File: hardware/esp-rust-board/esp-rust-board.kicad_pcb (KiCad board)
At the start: 2 copper layers, 22.9 x 63.5 mm, 96 parts, among them J1 USB4105-GF-A, Q1 DMG3415U, SW1 SW_Push, SW2 SW_Push, U1 SHTC3, U2 ICM-42670-P, U3 ESP32-C3-MINI-1, U4 Rust_Board, U5 SY8088, U6 MCP73831T-2ACI/OT, Y1 32.768Hz

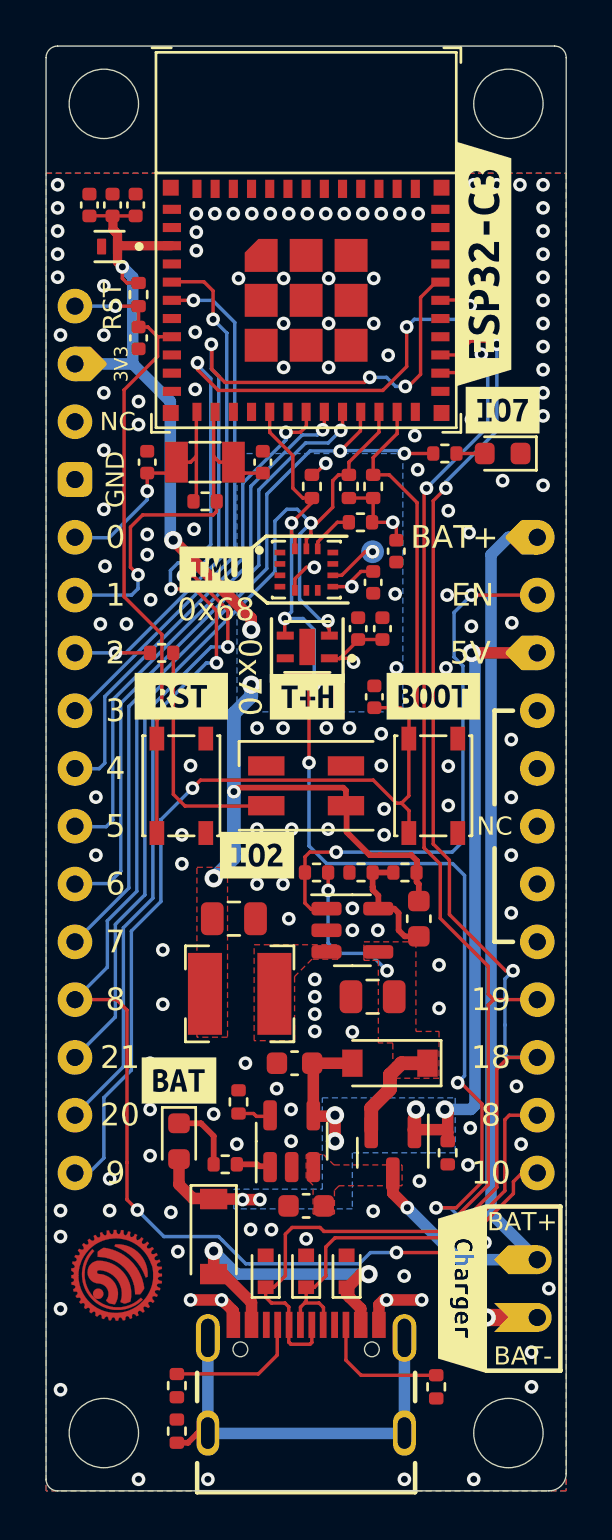
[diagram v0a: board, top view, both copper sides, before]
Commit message: Clean up, update symbols and footprints, port to Kicad 8.0
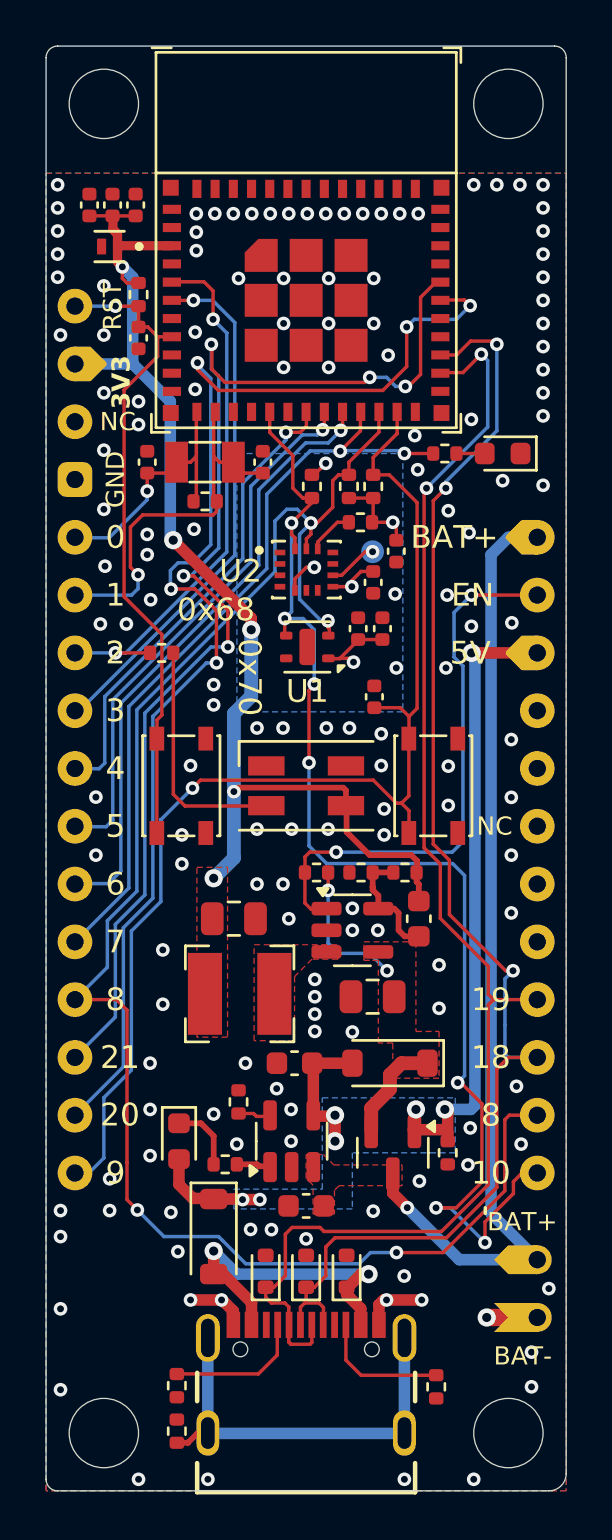
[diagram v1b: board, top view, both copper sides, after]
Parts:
- removed G***: LOGO, Rust_Board:esp-rs_logo_4mm
- removed G***: LOGO, Rust_Board:esp-rs_logo_tiny
- removed REF**: logo_HF, Rust_Board:logo_HF
- removed REF**: logo_HF, Rust_Board:logo_PB
- removed kibuzzard-61B9CCBB, kibuzzard-61B9CE3D, kibuzzard-61B9CE86, kibuzzard-61B9CEAB, kibuzzard-61B9EF98, kibuzzard-61C05335, kibuzzard-61C057D5, kibuzzard-61C057FD, kibuzzard-61C05804, kibuzzard-61C0588C, kibuzzard-61C05909, kibuzzard-61C05949, kibuzzard-61C05975, kibuzzard-61C0597E, kibuzzard-61C05A1A, kibuzzard-61C05A22, kibuzzard-61C05B60, kibuzzard-61C05BAC, kibuzzard-61C05C0D, kibuzzard-61C05C87, kibuzzard-61C05C92, kibuzzard-61C05D58, kibuzzard-61C05D75, kibuzzard-61C05DB0, kibuzzard-61C0F315, kibuzzard-61C0F325, kibuzzard-61C0F363, kibuzzard-61C0F3FF, kibuzzard-61C0F406, kibuzzard-61C0F511, kibuzzard-61C0F551: G***, label
- removed kibuzzard-61E1AB2E: G***, kibuzzard-61E1AB2E
- removed kibuzzard-61F26841: G***, kibuzzard-61F26841
- removed kibuzzard-61F26855: G***, kibuzzard-61F26855
- removed kibuzzard-61F2685B: G***, kibuzzard-61F2685B
- removed kibuzzard-623DAB98: G***, kibuzzard-623DAB98
- removed kibuzzard-6269032F: G***, kibuzzard-6269032F
- U1: footprint Rust_Board:SON100P200X200X80-5N -> Sensor_Humidity:Sensirion_DFN-4-1EP_2x2mm_P1mm_EP0.7x1.6mm
- U3: footprint Espressif:ESP32-C3-MINI-1 -> Rust_Board:ESP32-C3-MINI-1
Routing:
- net +3V3: track 63.0 -> 65.4 mm, vias 11 -> 10
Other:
- board text removed: "2217"
- board text removed: "ESP-RS"
- board text removed: "ESP32-C3-DevKit-RUST-1 v1.2a 04/2022"
- board text removed: "I2C Sensors IMU 0x68 T+H 0x70 SDA GPIO10 SCL GPIO8"
- board text removed: "Li-Ion only!"
- board text removed: "github.com/esp-rs"

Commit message: Solve remaining  errors and warnings
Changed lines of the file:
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@@
 		(at 148.092 88.034)
 		(property "Reference" "U2"
-			(at -2.892 0.066 0)
+			(at -2.092 -2.334 0)
 			(layer "F.SilkS")
 			(effects
@@
 			)
 		)
-		(property "Footprint" "Rust_Board:IC_ICM-42670-P"
+		(property "Footprint" "IC_ICM-42670-P"
 			(at 0 0 0)
 			(layer "F.Fab")
@@
 			(net 1 "GND")
 			(pinfunction "AP_SDO/AP_AD0")
-			(pintype "bidirectional")
+			(pintype "power_in")
 		)
 		(pad "2" smd rect
@@
 			)
 		)
-		(property "Description" ""
+		(property "Description" "Single cell, Li-Ion/Li-Po charge management controller, 4.20V, Tri-State Status Output, in SOT23-5 package"
 			(at 0 0 90)
 			(layer "F.Fab")
@@
 			(net 30 "Net-(U6-STAT)")
 			(pinfunction "STAT")
-			(pintype "output")
+			(pintype "tri_state")
 		)
 		(pad "2" smd roundrect
@@
 			(roundrect_rratio 0.25)
 			(net 1 "GND")
-			(pinfunction "VSS")
+			(pinfunction "V_{SS}")
 			(pintype "power_in")
 		)
@@
 			(roundrect_rratio 0.25)
 			(net 9 "+BATT")
-			(pinfunction "VBAT")
+			(pinfunction "V_{BAT}")
 			(pintype "power_out")
 		)
@@
 			(roundrect_rratio 0.25)
 			(net 8 "VBUS")
-			(pinfunction "VDD")
+			(pinfunction "V_{DD}")
 			(pintype "power_in")
 		)
@@
 			)
 		)
-		(property "Description" ""
+		(property "Description" "-3A Id, -20V Vds, P-Channel MOSFET, SOT-23"
 			(at 0 0 -90)
 			(layer "F.Fab")

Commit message: Update package
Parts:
- U2: footprint Rust_Board:IC_ICM-42670-P -> Package_LGA:LGA-14_3x2.5mm_P0.5mm_LayoutBorder3x4y

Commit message: Update esp-rust-board.kicad_pcb
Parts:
- D1: footprint Rust_Board:SOD-882 -> Diode_SMD:D_SOD-882
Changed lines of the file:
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@@
 		)
 	)
-	(footprint "Rust_Board:SOD-882"
+	(footprint "Diode_SMD:D_SOD-882"
 		(layer "F.Cu")
 		(at 139.442 73.834 180)
+		(descr "SOD-882, DFN1006-2, body 1.0 x 0.6 x 0.48mm, pitch 0.65mm, https://assets.nexperia.com/documents/package-information/SOD882.pdf")
+		(tags "Diode SOD882 DFN1006-2")
 		(property "Reference" "D1"
-			(at 0.116 -1.0032 0)
-			(layer "F.SilkS")
-			(hide yes)
-			(effects
-				(font
-					(size 0.32 0.32)
-					(thickness 0.08)
+			(at 1.442 0.034 -90)
+			(layer "F.SilkS")
+			(effects
+				(font
+					(size 1 1)
+					(thickness 0.15)
 				)
 			)
 		)
 		(property "Value" "LESD8D3.3CAT5G"
-			(at 2.5544 1.1032 0)
-			(layer "F.Fab")
-			(hide yes)
-			(effects
-				(font
-					(size 0.32 0.32)
-					(thickness 0.08)
-				)
-			)
-		)
-		(property "Footprint" "Rust_Board:SOD-882"
+			(at 0 1.35 180)
+			(layer "F.Fab")
+			(effects
+				(font
+					(size 1 1)
+					(thickness 0.15)
+				)
+			)
+		)
+		(property "Footprint" "Diode_SMD:D_SOD-882"
 			(at 0 0 180)
+			(unlocked yes)
 			(layer "F.Fab")
 			(hide yes)
@@
 		(property "Datasheet" ""
 			(at 0 0 180)
+			(unlocked yes)
 			(layer "F.Fab")
 			(hide yes)
@@
 		(property "Description" ""
 			(at 0 0 180)
+			(unlocked yes)
 			(layer "F.Fab")
 			(hide yes)
@@
 		(sheetfile "esp-rust-board.kicad_sch")
 		(attr smd)
-		(fp_poly
-			(pts
-				(xy 0.2 -0.3) (xy 0.5 -0.3) (xy 0.5 0.3) (xy 0.2 0.3)
-			)
-			(stroke
-				(width 0.01)
-				(type solid)
-			)
-			(fill solid)
-			(layer "F.Paste")
-		)
-		(fp_poly
-			(pts
-				(xy -0.5 -0.3) (xy -0.2 -0.3) (xy -0.2 0.3) (xy -0.5 0.3)
-			)
-			(stroke
-				(width 0.01)
-				(type solid)
-			)
-			(fill solid)
-			(layer "F.Paste")
-		)
-		(fp_line
-			(start 0.65 0.67)
-			(end -0.65 0.67)
-			(stroke
-				(width 0.127)
-				(type solid)
-			)
-			(layer "F.SilkS")
-		)
-		(fp_line
-			(start -0.65 -0.67)
-			(end 0.65 -0.67)
-			(stroke
-				(width 0.127)
-				(type solid)
-			)
-			(layer "F.SilkS")
-		)
-		(fp_circle
-			(center -1.3 0)
-			(end -1.2 0)
-			(stroke
-				(width 0.2)
-				(type solid)
-			)
-			(fill none)
-			(layer "F.SilkS")
-		)
-		(fp_poly
-			(pts
-				(xy 0.100009 -0.4) (xy 0.6 -0.4) (xy 0.6 0.400031) (xy 0.100009 0.400031)
-			)
-			(stroke
-				(width 0.01)
-				(type solid)
-			)
-			(fill solid)
-			(layer "F.Mask")
-		)
-		(fp_poly
-			(pts
-				(xy -0.600941 -0.4) (xy -0.1 -0.4) (xy -0.1 0.400628) (xy -0.600941 0.400628)
-			)
-			(stroke
-				(width 0.01)
-				(type solid)
-			)
-			(fill solid)
-			(layer "F.Mask")
-		)
-		(fp_line
-			(start 0.9 0.7)
-			(end 0.9 -0.7)
-			(stroke
-				(width 0.05)
-				(type solid)
-			)
-			(layer "F.CrtYd")
-		)
-		(fp_line
-			(start 0.9 -0.7)
-			(end -0.9 -0.7)
-			(stroke
-				(width 0.05)
-				(type solid)
-			)
-			(layer "F.CrtYd")
-		)
-		(fp_line
-			(start -0.9 0.7)
-			(end 0.9 0.7)
-			(stroke
-				(width 0.05)
-				(type solid)
-			)
-			(layer "F.CrtYd")
-		)
-		(fp_line
-			(start -0.9 -0.7)
-			(end -0.9 0.7)
-			(stroke
-				(width 0.05)
-				(type solid)
-			)
-			(layer "F.CrtYd")
-		)
-		(fp_line
-			(start 0.65 0.45)
-			(end -0.65 0.45)
-			(stroke
-				(width 0.127)
-				(type solid)
-			)
-			(layer "F.Fab")
-		)
-		(fp_line
-			(start 0.65 -0.45)
-			(end 0.65 0.45)
-			(stroke
-				(width 0.127)
-				(type solid)
-			)
-			(layer "F.Fab")
-		)
-		(fp_line
-			(start -0.65 0.45)
-			(end -0.65 -0.45)
-			(stroke
-				(width 0.127)
-				(type solid)
-			)
-			(layer "F.Fab")
-		)
-		(fp_line
-			(start -0.65 -0.45)
-			(end 0.65 -0.45)
-			(stroke
-				(width 0.127)
-				(type solid)
-			)
-			(layer "F.Fab")
-		)
-		(fp_circle
-			(center -1.3 0)
-			(end -1.2 0)
-			(stroke
-				(width 0.2)
-				(type solid)
-			)
-			(fill none)
-			(layer "F.Fab")
+		(fp_line
+			(start -0.81 0.61)
+			(end 0.5 0.61)
+			(stroke
+				(width 0.12)
+				(type solid)
+			)
+			(layer "F.SilkS")
+		)
+		(fp_line
+			(start -0.81 -0.61)
+			(end 0.5 -0.61)
+			(stroke
+				(width 0.12)
+				(type solid)
+			)
+			(layer "F.SilkS")
+		)
+		(fp_line
+			(start -0.81 -0.61)
+			(end -0.81 0.61)
+			(stroke
+				(width 0.12)
+				(type solid)
+			)
+			(layer "F.SilkS")
+		)
+		(fp_line
+			(start 0.8 0.6)
+			(end -0.8 0.6)
+			(stroke
+				(width 0.05)
+				(type solid)
+			)
+			(layer "F.CrtYd")
+		)
+		(fp_line
+			(start 0.8 -0.6)
+			(end 0.8 0.6)
+			(stroke
+				(width 0.05)
+				(type solid)
+			)
+			(layer "F.CrtYd")
+		)
+		(fp_line
+			(start -0.8 -0.6)
+			(end 0.8 -0.6)
+			(stroke
+				(width 0.05)
+				(type solid)
+			)
+			(layer "F.CrtYd")
+		)
+		(fp_line
+			(start -0.8 -0.6)
+			(end -0.8 0.6)
+			(stroke
+				(width 0.05)
+				(type solid)
+			)
+			(layer "F.CrtYd")
+		)
+		(fp_line
+			(start 0.5 0.3)
+			(end -0.5 0.3)
+			(stroke
+				(width 0.1)
+				(type solid)
+			)
+			(layer "F.Fab")
+		)
+		(fp_line
+			(start 0.5 -0.3)
+			(end 0.5 0.3)
+			(stroke
+				(width 0.1)
+				(type solid)
+			)
+			(layer "F.Fab")
+		)
+		(fp_line
+			(start 0.15 0.2)
+			(end 0.15 -0.2)
+			(stroke
+				(width 0.1)
+				(type solid)
+			)
+			(layer "F.Fab")
+		)
+		(fp_line
+			(start 0.15 0)
+			(end 0.3 0)
+			(stroke
+				(width 0.1)
+				(type solid)
+			)
+			(layer "F.Fab")
+		)
+		(fp_line
+			(start 0.15 -0.2)
+			(end -0.15 0)
+			(stroke
+				(width 0.1)
+				(type solid)
+			)
+			(layer "F.Fab")
+		)
+		(fp_line
+			(start -0.15 0.2)
+			(end -0.15 -0.2)
+			(stroke
+				(width 0.1)
+				(type solid)
+			)
+			(layer "F.Fab")
+		)
+		(fp_line
+			(start -0.15 0)
+			(end 0.15 0.2)
+			(stroke
+				(width 0.1)
+				(type solid)
+			)
+			(layer "F.Fab")
+		)
+		(fp_line
+			(start -0.15 0)
+			(end -0.3 0)
+			(stroke
+				(width 0.1)
+				(type solid)
+			)
+			(layer "F.Fab")
+		)
+		(fp_line
+			(start -0.5 0.3)
+			(end -0.5 -0.3)
+			(stroke
+				(width 0.1)
+				(type solid)
+			)
+			(layer "F.Fab")
+		)
+		(fp_line
+			(start -0.5 -0.3)
+			(end 0.5 -0.3)
+			(stroke
+				(width 0.1)
+				(type solid)
+			)
+			(layer "F.Fab")
+		)
+		(fp_text user "${REFERENCE}"
+			(at -0.127 -1.35 180)
+			(layer "F.Fab")
+			(effects
+				(font
+					(size 1 1)
+					(thickness 0.15)
+				)
+			)
+		)
+		(pad "" smd roundrect
+			(at -0.35 0 180)
+			(size 0.3 0.6)
+			(layers "F.Paste")
+			(roundrect_rratio 0.1666666667)
+			(solder_paste_margin -0.05)
+		)
+		(pad "" smd roundrect
+			(at 0.35 0 180)
+			(size 0.3 0.6)
+			(layers "F.Paste")
+			(roundrect_rratio 0.1666666667)
+			(solder_paste_margin -0.05)
 		)
 		(pad "1" smd roundrect
 			(at -0.35 0 180)
 			(size 0.4 0.7)
-			(layers "F.Cu")
-			(roundrect_rratio 0.09)
+			(layers "F.Cu" "F.Mask")
+			(roundrect_rratio 0.125)
 			(net 2 "+3V3")
 			(pinfunction "A1")
 			(pintype "passive")
+			(solder_paste_margin -0.05)
 		)
 		(pad "2" smd roundrect
 			(at 0.35 0 180)
 			(size 0.4 0.7)
-			(layers "F.Cu")
-			(roundrect_rratio 0.09)
+			(layers "F.Cu" "F.Mask")
+			(roundrect_rratio 0.125)
 			(net 1 "GND")
 			(pinfunction "A2")
 			(pintype "passive")
-		)
-		(model "${RUST3D}/SOD-882.step"
+			(solder_paste_margin -0.05)
+		)
+		(model "${KICAD8_3DMODEL_DIR}/Diode_SMD.3dshapes/D_SOD-882.wrl"
 			(offset
 				(xyz 0 0 0)
@@
 			)
 			(rotate
-				(xyz -90 0 0)
-			)
-		)
+				(xyz 0 0 0)
+			)
+		)
